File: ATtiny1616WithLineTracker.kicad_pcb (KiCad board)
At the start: 2 copper layers, 85.6 x 78.2 mm, 28 parts, among them J1 Conn_02x04_Counter_Clockwise, J2 ATtiny_L, J3 Conn_01x08_Socket, J4 ATtiny_R, J5 Auriga_JST, J6 Conn_01x04_Socket, J7 Conn_01x04_Socket, J8 Conn_02x04_Counter_Clockwise, U1 ITR20001, U2 ITR20001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

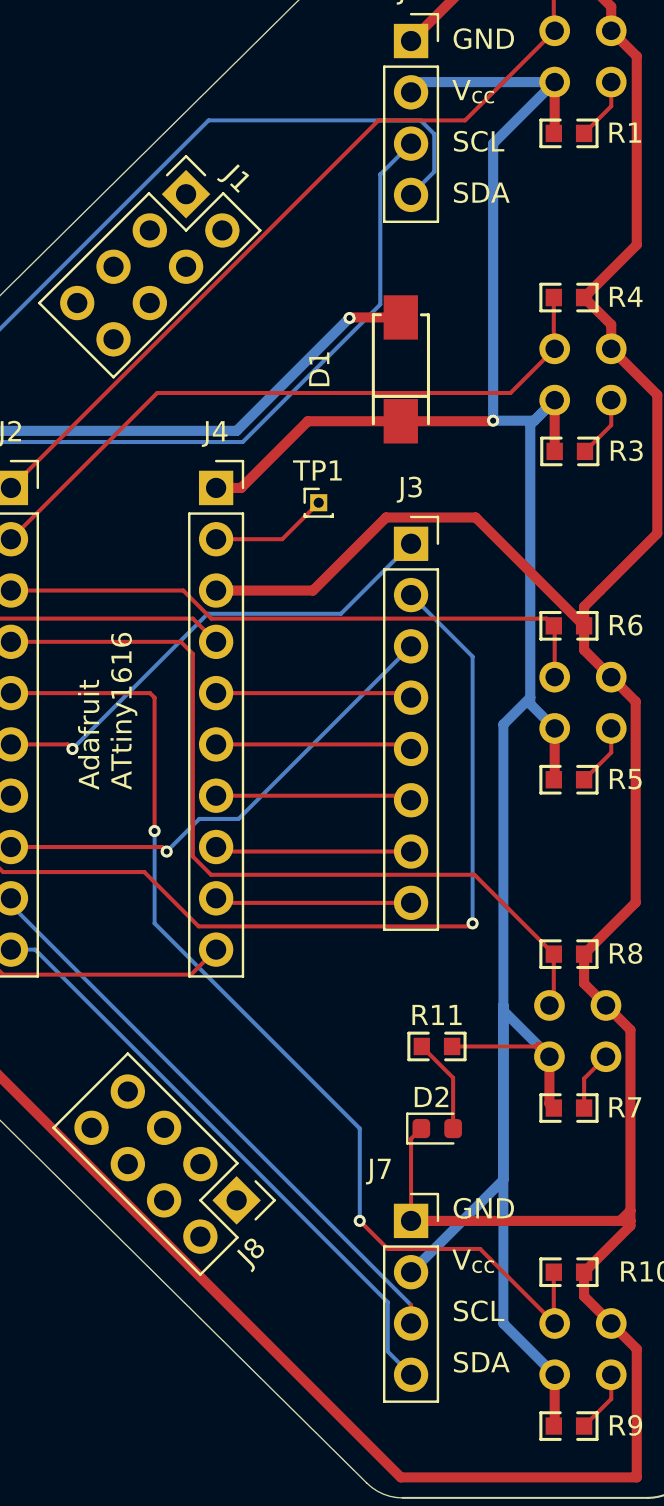
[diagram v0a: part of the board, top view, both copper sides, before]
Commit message: Fix SDA-SCL silk markings
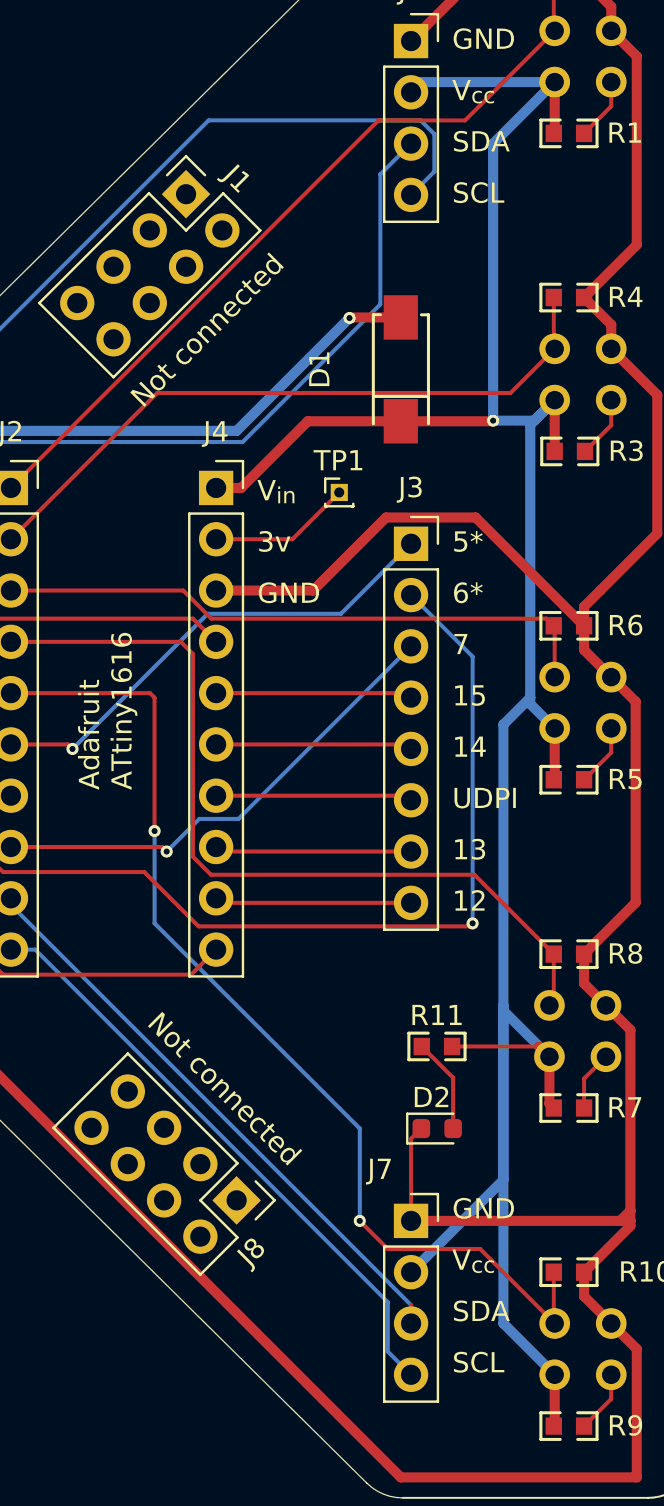
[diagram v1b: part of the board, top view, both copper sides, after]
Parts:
- moved TP1 1.14 mm to (179.3, 65.0)
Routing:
- net /3v: track 5.83 -> 7.06 mm
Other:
- board text added: "12"
- board text added: "13"
- board text added: "14"
- board text added: "15"
- board text added: "3v"
- board text added: "5*"
- board text added: "6*"
- board text added: "7"
- board text added: "GND"
- board text added: "Not connected"
- board text added: "UDPI"
- board text added: "V_{in}"
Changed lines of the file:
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@@
 			)
 		)
-		(fp_text user "SCL"
+		(fp_text user "SDA"
 			(at 2.032 5.08 0)
 			(unlocked yes)
@@
 			)
 		)
-		(fp_text user "SDA"
+		(fp_text user "SCL"
 			(at 2.032 7.62 0)
 			(unlocked yes)
@@
 			)
 		)
-		(fp_text user "SDA"
+		(fp_text user "SCL"
 			(at 2.032 8.128 0)
 			(unlocked yes)
@@
 			)
 		)
-		(fp_text user "SCL"
+		(fp_text user "SDA"
 			(at 2.032 5.588 0)
 			(unlocked yes)
@@
 	(footprint "Connector_PinHeader_1.00mm:PinHeader_1x01_P1.00mm_Vertical"
 		(layer "F.Cu")
-		(at 178.308 65.532)
+		(at 179.324 65.024)
 		(descr "Through hole straight pin header, 1x01, 1.00mm pitch, single row")
 		(tags "Through hole pin header THT 1x01 1.00mm single row")
@@
 		)
 	)
+	(gr_text "12"
+		(at 184.912 85.852 0)
+		(layer "F.SilkS")
+		(effects
+			(font
+				(size 1 1)
+				(thickness 0.1)
+			)
+			(justify left bottom)
+		)
+	)
 	(gr_text "Adafruit\nATtiny1616"
 		(at 169.164 79.756 90)
@@
 		)
 	)
+	(gr_text "UDPI"
+		(at 184.912 80.772 0)
+		(layer "F.SilkS")
+		(effects
+			(font
+				(size 1 1)
+				(thickness 0.1)
+			)
+			(justify left bottom)
+		)
+	)
+	(gr_text "6*"
+		(at 184.912 70.612 0)
+		(layer "F.SilkS")
+		(effects
+			(font
+				(size 1 1)
+				(thickness 0.1)
+			)
+			(justify left bottom)
+		)
+	)
+	(gr_text "V_{in}"
+		(at 175.26 65.532 0)
+		(layer "F.SilkS")
+		(effects
+			(font
+				(size 1 1)
+				(thickness 0.1)
+			)
+			(justify left bottom)
+		)
+	)
+	(gr_text "13"
+		(at 184.912 83.312 0)
+		(layer "F.SilkS")
+		(effects
+			(font
+				(size 1 1)
+				(thickness 0.1)
+			)
+			(justify left bottom)
+		)
+	)
+	(gr_text "14"
+		(at 184.912 78.232 0)
+		(layer "F.SilkS")
+		(effects
+			(font
+				(size 1 1)
+				(thickness 0.1)
+			)
+			(justify left bottom)
+		)
+	)
+	(gr_text "7"
+		(at 184.912 73.152 0)
+		(layer "F.SilkS")
+		(effects
+			(font
+				(size 1 1)
+				(thickness 0.1)
+			)
+			(justify left bottom)
+		)
+	)
+	(gr_text "5*"
+		(at 184.912 68.072 0)
+		(layer "F.SilkS")
+		(effects
+			(font
+				(size 1 1)
+				(thickness 0.1)
+			)
+			(justify left bottom)
+		)
+	)
+	(gr_text "15"
+		(at 184.912 75.692 0)
+		(layer "F.SilkS")
+		(effects
+			(font
+				(size 1 1)
+				(thickness 0.1)
+			)
+			(justify left bottom)
+		)
+	)
+	(gr_text "Not connected"
+		(at 169.672 91.44 -45)
+		(layer "F.SilkS")
+		(effects
+			(font
+				(size 1 1)
+				(thickness 0.1)
+			)
+			(justify left bottom)
+		)
+	)
+	(gr_text "GND"
+		(at 175.26 70.612 0)
+		(layer "F.SilkS")
+		(effects
+			(font
+				(size 1 1)
+				(thickness 0.1)
+			)
+			(justify left bottom)
+		)
+	)
+	(gr_text "Not connected"
+		(at 169.672 60.96 45)
+		(layer "F.SilkS")
+		(effects
+			(font
+				(size 1 1)
+				(thickness 0.1)
+			)
+			(justify left bottom)
+		)
+	)
+	(gr_text "3v"
+		(at 175.26 68.072 0)
+		(layer "F.SilkS")
+		(effects
+			(font
+				(size 1 1)
+				(thickness 0.1)
+			)
+			(justify left bottom)
+		)
+	)
 	(gr_text_box "Next version\n- Add silk for the pinouts..."
 		(start 214.884 61.976)
-		(end 236.22 78.74)
+		(end 255.016 78.74)
 		(layer "User.1")
 		(effects
@@
 	)
 	(segment
-		(start 176.5 67.34)
-		(end 178.308 65.532)
+		(start 177.008 67.34)
+		(end 179.324 65.024)
 		(width 0.2)
 		(layer "F.Cu")
@@
 	(segment
 		(start 173.228 67.34)
-		(end 176.5 67.34)
+		(end 177.008 67.34)
 		(width 0.2)
 		(layer "F.Cu")
